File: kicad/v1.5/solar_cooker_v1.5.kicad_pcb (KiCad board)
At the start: 2 copper layers, 160.5 x 77.1 mm, 20 parts, among them U1 microSD, U10 GPS, U2 clock_module, U3 anemometer, U4 AM2315, U5 BME680, U6 PT100, U7 pyranometer, U8 PT100, U9 PT100

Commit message: pcb minor fix
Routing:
- net GND: vias 28 -> 29
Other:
- board size 160.5 x 77.1 mm -> 160.5 x 77.2 mm
- board text added: "1 2 3"
- board text added: "Pt100_1"
- board text added: "Pt100_2"
- board text added: "Pt100_3"
- board text added: "connector"
- board text removed: "pt100_1"
- board text removed: "pt100_2"
- board text removed: "pt100_3"
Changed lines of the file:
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@@
     (property "ki_keywords" "R resistor")
     (attr smd)
-    (fp_text reference "R4" (at 0 -1.82) (layer "F.SilkS")
+    (fp_text reference "R4" (at 0 1.824) (layer "F.SilkS")
         (effects (font (size 1 1) (thickness 0.15)))
     )
@@
     (property "Sheetname" "")
     (attr through_hole)
-    (fp_text reference "U5" (at -7 -10.275 unlocked) (layer "F.SilkS")
+    (fp_text reference "U5" (at -7 -10.275 unlocked) (layer "F.SilkS") hide
         (effects (font (size 1 1) (thickness 0.1)))
     )
@@
         (effects (font (size 1 1) (thickness 0.1)))
     )
-    (fp_text value "GPS" (at -3 0.11 180 unlocked) (layer "F.SilkS")
+    (fp_text value "GPS" (at -3 0.11 180 unlocked) (layer "F.SilkS") hide
         (effects (font (size 1 1) (thickness 0.15)))
     )
@@
         (effects (font (size 1 1) (thickness 0.1)))
     )
-    (fp_text value "microSD" (at 0 2.54 180 unlocked) (layer "F.SilkS")
+    (fp_text value "microSD" (at 0 2.54 180 unlocked) (layer "F.SilkS") hide
         (effects (font (size 1 1) (thickness 0.15)))
     )
@@
         (effects (font (size 1 1) (thickness 0.1)))
     )
-    (fp_text value "clock_module" (at 0.05 5.32 unlocked) (layer "F.SilkS")
+    (fp_text value "clock_module" (at 0.05 5.32 unlocked) (layer "F.SilkS") hide
         (effects (font (size 1 1) (thickness 0.15)))
     )
@@
     (property "Sheetname" "")
     (attr through_hole)
-    (fp_text reference "A1" (at -23.525 -53.945 -90) (layer "F.SilkS")
-        (effects (font (size 1 1) (thickness 0.15)))
-    )
-    (fp_text value "A000067" (at -17.175 52.075 -90) (layer "F.Fab")
+    (fp_text reference "A1" (at -23.525 -53.945 90) (layer "User.1") hide
+        (effects (font (size 1 1) (thickness 0.15)))
+    )
+    (fp_text value "A000067" (at -17.175 52.075 90) (layer "F.Fab")
         (effects (font (size 1 1) (thickness 0.15)))
     )
@@
     (property "Sheetname" "")
     (attr through_hole)
-    (fp_text reference "S1" (at -3.175 -4.445 180) (layer "F.SilkS")
+    (fp_text reference "S1" (at 5.6246 4.1 180) (layer "F.SilkS")
         (effects (font (size 1 1) (thickness 0.15)))
     )
@@
   (gr_line (start 99.95 123.3) (end 77.95 123.3)
     (stroke (width 0.15) (type default)) (layer "F.SilkS"))
-  (gr_line (start 75.55 80.125) (end 70.1 80.125)
+  (gr_line (start 75.55 80.125) (end 70.2 80.125)
     (stroke (width 0.15) (type default)) (layer "F.SilkS"))
   (gr_line (start 75.55 105.525) (end 75.55 80.125)
@@
   (gr_line (start 75.55 132.025) (end 75.55 106.625)
     (stroke (width 0.15) (type default)) (layer "F.SilkS"))
-  (gr_line (start 75.55 106.625) (end 70.1 106.625)
+  (gr_line (start 75.65 106.625) (end 70.3 106.625)
     (stroke (width 0.15) (type default)) (layer "F.SilkS"))
   (gr_line (start 77.95 123.3) (end 77.95 157.1)
@@
   (gr_line (start 102.55 140.1) (end 102.55 157.1)
     (stroke (width 0.15) (type default)) (layer "F.SilkS"))
-  (gr_line (start 70.1 132.025) (end 75.55 132.025)
+  (gr_line (start 70.3 132.025) (end 75.55 132.025)
     (stroke (width 0.15) (type default)) (layer "F.SilkS"))
   (gr_line (start 75.55 133.125) (end 75.55 157.1)
@@
   (gr_line (start 99.95 157.1) (end 99.95 123.3)
     (stroke (width 0.15) (type default)) (layer "F.SilkS"))
-  (gr_line (start 70.1 105.525) (end 75.55 105.525)
+  (gr_line (start 70.3 105.525) (end 75.55 105.525)
     (stroke (width 0.15) (type default)) (layer "F.SilkS"))
   (gr_line (start 102.55 140.1) (end 118.9 140.1)
     (stroke (width 0.15) (type default)) (layer "F.SilkS"))
-  (gr_line (start 70.1 133.125) (end 75.55 133.125)
+  (gr_line (start 70.3 133.125) (end 75.55 133.125)
     (stroke (width 0.15) (type default)) (layer "F.SilkS"))
-  (gr_rect (start 70.1 80) (end 230.58 157.1)
+  (gr_rect (start 70.1 80) (end 230.58 157.2)
     (stroke (width 0.1) (type default)) (fill none) (layer "Edge.Cuts"))
   (gr_rect (start 20 15) (end 280 165)
@@
   (gr_rect (start 21.5 16.4) (end 171.5 76.4)
     (stroke (width 0.2) (type default)) (fill none) (layer "User.1"))
-  (gr_text "black" (at 152.125 148.75) (layer "F.SilkS")
+  (gr_text "black" (at 152.2 153.2 -90) (layer "F.SilkS")
     (effects (font (size 1 1) (thickness 0.15)))
   )
@@
     (effects (font (size 1.5 1.5) (thickness 0.3) bold) (justify left bottom))
   )
-  (gr_text "white" (at 142.2 148.75) (layer "F.SilkS")
+  (gr_text "white" (at 142 153.128571 -90) (layer "F.SilkS")
     (effects (font (size 1 1) (thickness 0.15)))
   )
-  (gr_text "red" (at 147.1 148.75) (layer "F.SilkS")
+  (gr_text "red" (at 147 152.390476 -90) (layer "F.SilkS")
     (effects (font (size 1 1) (thickness 0.15)))
   )
@@
     (effects (font (size 2 2) (thickness 0.3)) (justify left bottom))
   )
-  (gr_text "white" (at 193.825 148.75) (layer "F.SilkS")
+  (gr_text "white" (at 193.7 153.128571 -90) (layer "F.SilkS")
     (effects (font (size 1 1) (thickness 0.15)))
   )
-  (gr_text "blue" (at 175.525 148.75) (layer "F.SilkS")
+  (gr_text "connector" (at 212.7 149.8) (layer "F.SilkS")
+    (effects (font (size 1 1) (thickness 0.15)) (justify left bottom))
+  )
+  (gr_text "blue" (at 175.5 152.795238 -90) (layer "F.SilkS")
     (effects (font (size 1 1) (thickness 0.15)))
   )
-  (gr_text "yellow" (at 188.65 148.75) (layer "F.SilkS")
+  (gr_text "yellow" (at 188.7 153.509524 -90) (layer "F.SilkS")
     (effects (font (size 1 1) (thickness 0.15)))
   )
-  (gr_text "brown" (at 165.35 148.75) (layer "F.SilkS")
+  (gr_text "brown" (at 165.3 153.390476 -90) (layer "F.SilkS")
     (effects (font (size 1 1) (thickness 0.15)))
   )
-  (gr_text "blue" (at 198.725 148.75) (layer "F.SilkS")
+  (gr_text "blue" (at 198.9 152.795238 -90) (layer "F.SilkS")
     (effects (font (size 1 1) (thickness 0.15)))
   )
@@
     (effects (font (size 2 2) (thickness 0.3)) (justify left bottom))
   )
-  (gr_text "red" (at 183.55 148.75) (layer "F.SilkS")
+  (gr_text "red" (at 183.5 152.390476 -90) (layer "F.SilkS")
     (effects (font (size 1 1) (thickness 0.15)))
   )
-  (gr_text "LCD display" (at 207.325 149.2) (layer "F.SilkS")
+  (gr_text "LCD display" (at 207.3 145) (layer "F.SilkS")
     (effects (font (size 2 2) (thickness 0.3)) (justify left bottom))
+  )
+  (gr_text "1 2 3" (at 77.8 80.9 -90) (layer "F.SilkS")
+    (effects (font (size 1 1) (thickness 0.15)) (justify left bottom))
   )
   (gr_text "OFF" (at 115.9 133.3 -90) (layer "F.SilkS")
     (effects (font (size 1.5 1.5) (thickness 0.3) bold) (justify left bottom))
   )
-  (gr_text "pt100_2" (at 71.75 119.1 -90) (layer "F.SilkS")
+  (gr_text "Pt100_2" (at 71.6 119.7 270) (layer "F.SilkS")
     (effects (font (size 1 1) (thickness 0.15)))
   )
-  (gr_text "pt100_1" (at 71.675 92.175 -90) (layer "F.SilkS")
+  (gr_text "Pt100_1" (at 71.7 92.8 270) (layer "F.SilkS")
     (effects (font (size 1 1) (thickness 0.15)))
   )
-  (gr_text "pt100_3" (at 71.675 144.975 -90) (layer "F.SilkS")
+  (gr_text "Pt100_3" (at 71.6 146.2 270) (layer "F.SilkS")
     (effects (font (size 1 1) (thickness 0.15)))
   )
-  (gr_text "black" (at 170.5 148.75) (layer "F.SilkS")
+  (gr_text "black" (at 170.4 153.2 -90) (layer "F.SilkS")
     (effects (font (size 1 1) (thickness 0.15)))
   )
@@
     (effects (font (size 2 2) (thickness 0.3)) (justify left bottom))
   )
-  (gr_text "clear" (at 157.275 148.75) (layer "F.SilkS")
+  (gr_text "clear" (at 157.2 153.080953 -90) (layer "F.SilkS")
     (effects (font (size 1 1) (thickness 0.15)))
   )
@@
   (via (at 210.1 134.8) (size 0.8) (drill 0.4) (layers "F.Cu" "B.Cu") (free) (net 2))
   (via (at 114.44 122.44) (size 0.8) (drill 0.4) (layers "F.Cu" "B.Cu") (free) (net 2))
+  (via (at 202 117.2) (size 0.8) (drill 0.4) (layers "F.Cu" "B.Cu") (free) (net 2))
   (via (at 138.54 90.06) (size 0.8) (drill 0.4) (layers "F.Cu" "B.Cu") (free) (net 2))
   (via (at 126.1 117.8) (size 0.8) (drill 0.4) (layers "F.Cu" "B.Cu") (free) (net 2))
@@
     (connect_pads (clearance 0.5))
     (min_thickness 0.25) (filled_areas_thickness no)
-    (fill (thermal_gap 0.5) (thermal_bridge_width 0.5))
+    (fill yes (thermal_gap 0.5) (thermal_bridge_width 0.5))
     (polygon
       (pts
         (xy 70.0846 79.96)
-        (xy 230.326 79.706)
-        (xy 230.326 156.846)
-        (xy 70.0846 157.1)
+        (xy 230.6 80)
+        (xy 230.6 157.2)
+        (xy 70.1 157.2)
       )
     )

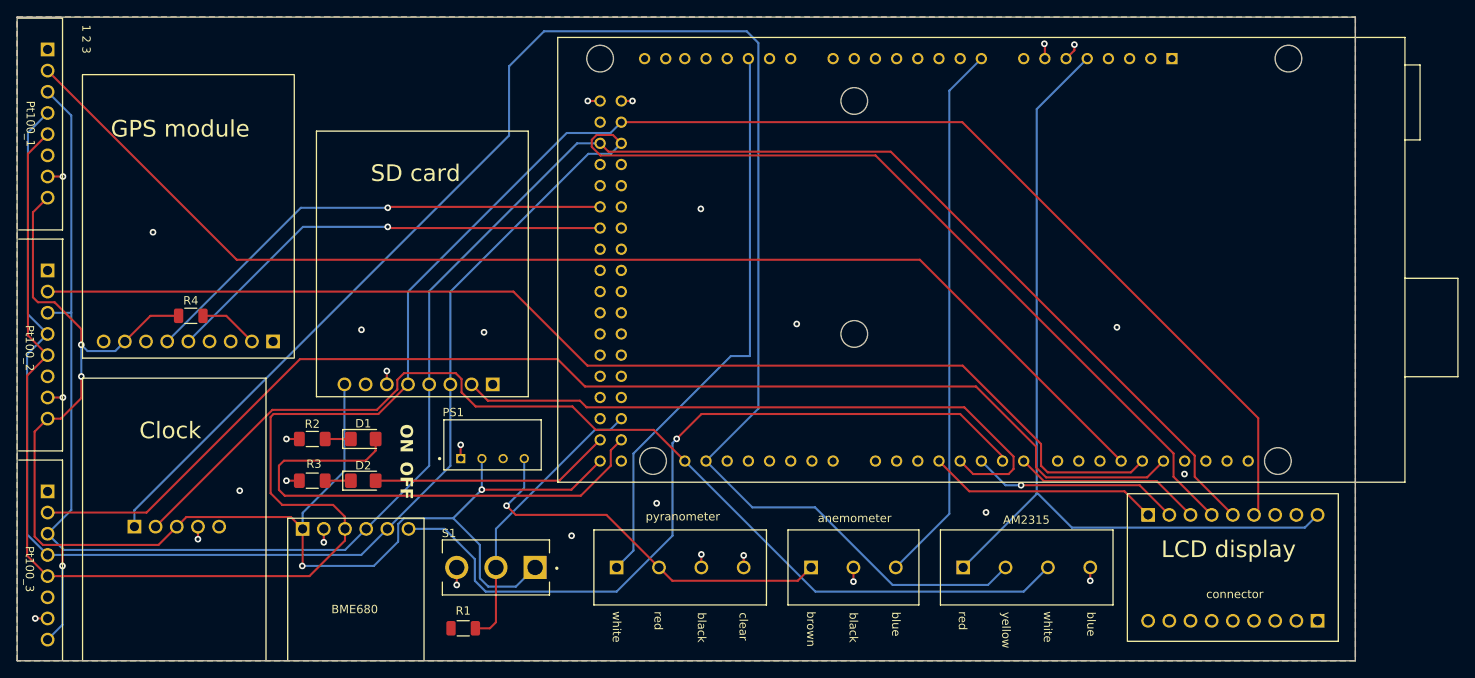
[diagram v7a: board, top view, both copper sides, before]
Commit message: silkscreen fix for order v1
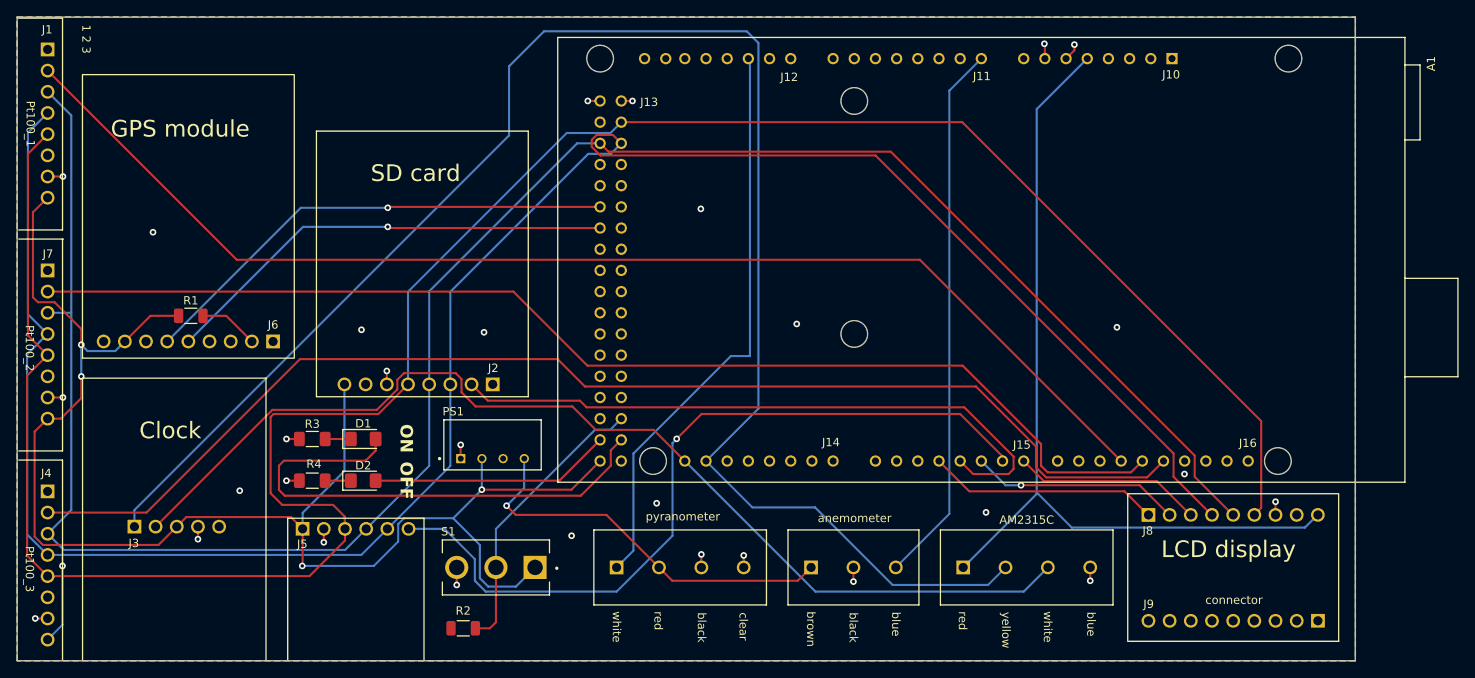
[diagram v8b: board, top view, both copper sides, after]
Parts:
- removed U11: ~, custom_components:display
- removed U8, U9: PT100, custom_components:PT100
- added J4: Pt100, custom_components:Pt100, F.Cu at (57.8, 145.8)
- added J7: Pt100, custom_components:Pt100, F.Cu at (57.8, 119.3)
- added J8: display, custom_components:display, F.Cu at (215.9, 144.8)
- D1: value LED_GREEN -> LED
- D2: value LED_RED -> LED
- J1: renamed from U6; value PT100 -> Pt100; footprint custom_components:PT100 -> custom_components:Pt100
- R1: renamed from R4; value 10k -> R_Small
- R2: renamed from R1; value 10k -> R_Small
- R3: renamed from R2; value 150 -> R_Small
- R4: renamed from R3; value 150 -> R_Small
- U2: renamed from U4; value AM2315 -> AM2315C
- renumbered U1 to J2, U2 to J3, U5 to J5, U10 to J6, U3 to U1, U7 to U3
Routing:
- net GND: track 29.8 -> 31.3 mm, vias 29 -> 30
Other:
- board text added: "J10"
- board text added: "J11"
- board text added: "J12"
- board text added: "J13"
- board text added: "J14"
- board text added: "J15"
- board text added: "J16"
- board text added: "J9"
- board text added: "solar cooker testing station v1"
